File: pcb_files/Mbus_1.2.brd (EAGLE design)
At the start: 101.6 x 71.1 mm, 50 parts, among them IC1 NCP1117ST50T3G, IC3 ATMEGA2560-16AU, IC4 RTC_PCF8523T, J1 F-1X18-SIP-100-32Y, J2 USB_A_SMT_FEMALE, M1 SERVO, Q1 BSS138, Q2 32.768, Q3 BSS138, Y1 CSTCE16M0V53-R0 16MHZ

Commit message: Modify the npn transistor and board layout for 1.2
Signed-off-by: Yiteng Cai <alonsochate@umich.edu>
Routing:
- net PD7: track 121.3 -> 46.4 mm, vias 2 -> 0
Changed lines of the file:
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@@
 <drawing>
 <settings>
-<setting alwaysvectorfont="no"/>
+<setting alwaysvectorfont="yes"/>
 <setting keepoldvectorfont="yes"/>
 <setting verticaltext="up"/>
@@
 <wire x1="96.57588125" y1="36.41851875" x2="96.57588125" y2="34.65321875" width="0.2032" layer="1"/>
 <wire x1="97.6376" y1="35.3568" x2="98.552" y2="35.306" width="0.2032" layer="1"/>
-<wire x1="13.1064" y1="18.1864" x2="13.1064" y2="17.26235625" width="0.2032" layer="1"/>
-<wire x1="13.8176" y1="18.8976" x2="13.1064" y2="18.1864" width="0.2032" layer="1"/>
-<wire x1="13.8176" y1="19.1008" x2="13.8176" y2="18.8976" width="0.2032" layer="1"/>
-<wire x1="35.9664" y1="19.1008" x2="13.8176" y2="19.1008" width="0.2032" layer="16"/>
-<wire x1="68.7832" y1="51.9176" x2="35.9664" y2="19.1008" width="0.2032" layer="16"/>
-<wire x1="71.3232" y1="51.9176" x2="68.7832" y2="51.9176" width="0.2032" layer="16"/>
-<wire x1="71.9328" y1="52.5272" x2="71.3232" y2="51.9176" width="0.2032" layer="1"/>
-<wire x1="72.7456" y1="52.5272" x2="71.9328" y2="52.5272" width="0.2032" layer="1"/>
 <wire x1="72.7456" y1="52.5272" x2="72.77" y2="52.482" width="0.2032" layer="1"/>
-<via x="13.8176" y="19.1008" extent="1-16" drill="0.4064"/>
-<via x="71.3232" y="51.9176" extent="1-16" drill="0.4064"/>
 </signal>
 <signal name="+3V3">

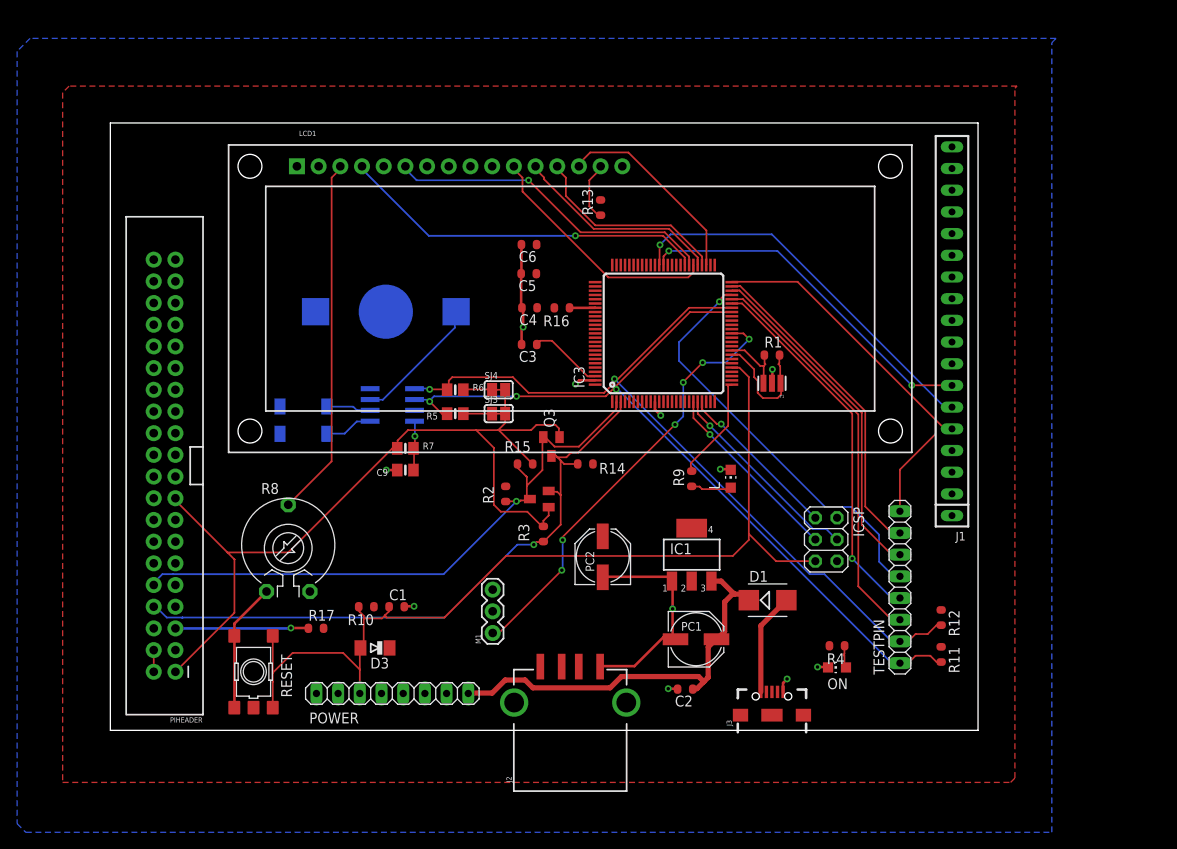
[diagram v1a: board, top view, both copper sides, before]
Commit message: Modify trace width. Not finished on the board layout.
Signed-off-by: Yiteng Cai <alonsochate@umich.edu>
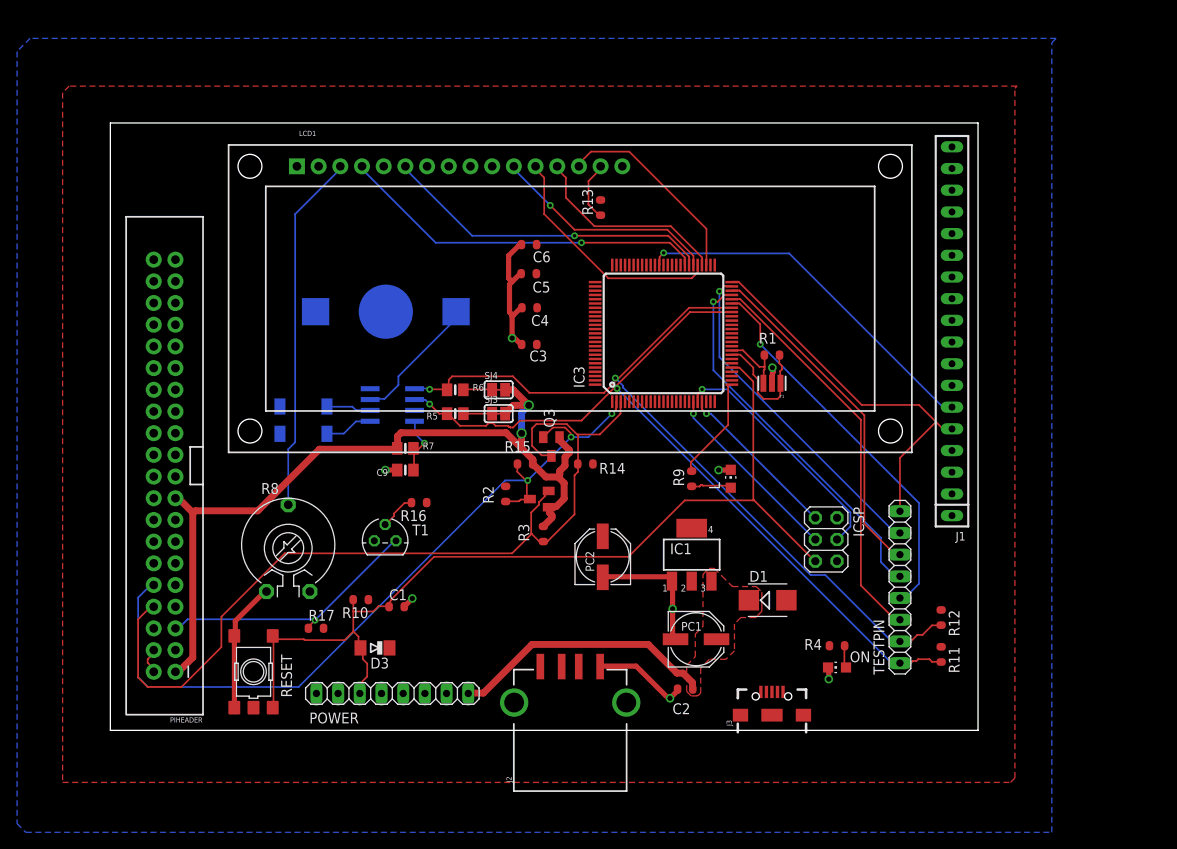
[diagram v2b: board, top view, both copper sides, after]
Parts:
- removed M1: SERVO, SparkFun-Electromechanical:1X03
- added T1: 2N3904, transistor:TO92
- moved R16 28.3 mm to (36.2, 26.7)
- moved R10 1.05 mm to (29.3, 15.3)
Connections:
- net +5V: no longer M1.2
- net GND: now also T1.3; no longer M1.3
- net N$4: now also T1.2
- net OUT: now also T1.1
- net PL3: no longer M1.1
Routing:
- net PL3: track 51.2 -> 0.00 mm, vias 6 -> 0
- net RXD3: track 41.6 -> 0.00 mm, vias 2 -> 0
- net TXD0: track 76.1 -> 105.8 mm, vias 1 -> 0
- net RXD0: track 72.9 -> 95.2 mm, vias 1 -> 3
- net VIN: track 48.2 -> 31.3 mm
- net OUT: track 15.6 -> 31.6 mm
- net PWRIN: track 12.0 -> 0.00 mm
- net AREF: track 8.76 -> 0.00 mm
- net +3V3: track 103.3 -> 97.8 mm, vias 0 -> 2
- net PB2: track 23.8 -> 28.8 mm
- net PD4: track 49.0 -> 44.1 mm
- net N$4: track 0.00 -> 4.37 mm
- net PC2: track 24.7 -> 28.3 mm
- net N$1: track 3.01 -> 0.00 mm
- net TXD3: track 45.5 -> 42.9 mm
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- added copper zone on layer 1, net VIN

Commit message: Save
Signed-off-by: Yiteng Cai <alonsochate@umich.edu>
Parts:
- moved R2 10.6 mm to (52.3, 36.4)
- moved R3 8.99 mm to (45.8, 30.5)
- moved Q3 6.35 mm to (56.7, 29.3), turned to 270 degrees
- moved R14 5.70 mm to (60.4, 34.3)
- moved R15 5.58 mm to (52.4, 27.2), turned to 90 degrees
- moved Q1 5.25 mm to (50.2, 32.3), turned to 270 degrees
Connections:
- new net N$12: PIHEADER.10, Q3.2, R15.1
- new net N$5: PIHEADER.8, Q1.2, R3.1
- net RXD0: no longer PIHEADER.10, Q3.2, R15.1
- net TXD0: no longer PIHEADER.8, Q1.2, R3.1
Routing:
- net TXD0: track 105.8 -> 5.75 mm
- net RXD0: track 95.2 -> 3.66 mm, vias 3 -> 0
- net N$12: track 0.00 -> 75.7 mm, vias 0 -> 1
- net N$5: track 0.00 -> 73.8 mm
- net TXD1: track 46.6 -> 0.00 mm
- net RXD1: track 45.4 -> 0.00 mm, vias 1 -> 0
- net PD4: track 44.1 -> 0.00 mm, vias 1 -> 0
- net PC5: track 43.3 -> 0.00 mm, vias 1 -> 0
- net TXD3: track 42.9 -> 0.00 mm, vias 1 -> 0
- net PD5: track 40.0 -> 0.00 mm
- net PD6: track 39.1 -> 0.00 mm, vias 1 -> 0
- net PC4: track 38.8 -> 0.00 mm, vias 1 -> 0
- net PB2: track 28.8 -> 0.00 mm, vias 1 -> 0
- net PC2: track 28.3 -> 0.00 mm
- net +3V3: track 97.8 -> 70.4 mm, vias 2 -> 0
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- added copper zone on layer 1, net +3V3

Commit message: Save
Signed-off-by: Yiteng Cai <alonsochate@umich.edu>
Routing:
- net TXD1: track 0.00 -> 48.9 mm, vias 0 -> 1
- net PD4: track 0.00 -> 44.0 mm, vias 0 -> 1
- net RXD1: track 0.00 -> 43.9 mm
- net PC5: track 0.00 -> 43.3 mm, vias 0 -> 1
- net TXD3: track 0.00 -> 42.9 mm, vias 0 -> 1
- net RXD3: track 0.00 -> 40.1 mm, vias 0 -> 2
- net PD5: track 0.00 -> 40.0 mm
- net PD6: track 0.00 -> 39.2 mm, vias 0 -> 1
- net PC4: track 0.00 -> 38.8 mm, vias 0 -> 1
- net N$1: track 0.00 -> 33.2 mm, vias 0 -> 2
- net SCL: track 77.1 -> 108.0 mm, vias 1 -> 2
- net PC2: track 0.00 -> 29.2 mm
- net PB2: track 0.00 -> 28.8 mm, vias 0 -> 1
- net RESET: track 88.0 -> 115.3 mm
- net PC3: track 0.00 -> 26.7 mm, vias 0 -> 1
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
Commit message: Create gerber files
Signed-off-by: Yiteng Cai <alonsochate@umich.edu>
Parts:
- moved C5 7.73 mm to (53.5, 59.8)
- moved IC3 7.73 mm to (69.3, 52.8)
- moved LCD1 7.73 mm to (58.3, 56.8)
- moved Q1 7.73 mm to (54.7, 38.6)
- moved R9 7.73 mm to (72.6, 35.8)
- moved C1 7.73 mm to (38.0, 20.8)
- moved C2 7.73 mm to (71.8, 11.1)
- moved C9 7.73 mm to (39.0, 36.8)
- moved D3 7.73 mm to (35.5, 15.9)
- moved ICSP 7.73 mm to (88.3, 28.6)
- moved ON 7.73 mm to (89.6, 13.7)
- moved PC1 7.73 mm to (73.1, 17.0)
- moved R11 7.73 mm to (101.8, 15.2)
- moved R15 7.73 mm to (56.9, 33.4)
- moved R17 7.73 mm to (28.6, 18.2)
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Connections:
- removed net RXD2: IC3.12
- removed net TXD2: IC3.13
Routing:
- net OUT: track 37.5 -> 89.9 mm
- net N$12: track 75.7 -> 60.3 mm
- net +3V3: track 71.3 -> 80.5 mm
- net GND: track 92.4 -> 100.6 mm
- net PWRIN: track 12.0 -> 18.2 mm
- net N$5: track 71.3 -> 69.1 mm
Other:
- board size 101.6 x 71.1 mm -> 113 x 78.7 mm

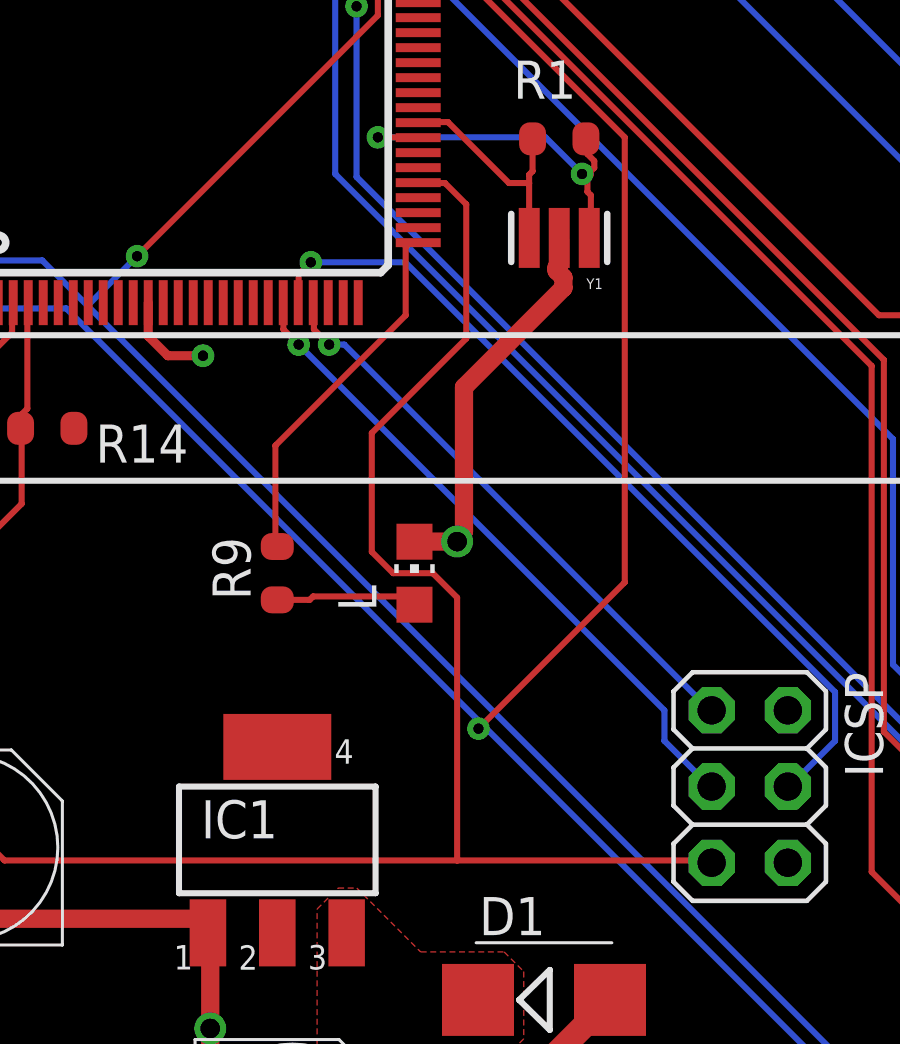
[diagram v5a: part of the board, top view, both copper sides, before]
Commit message: Modify one trace
Signed-off-by: Yiteng Cai <alonsochate@umich.edu>
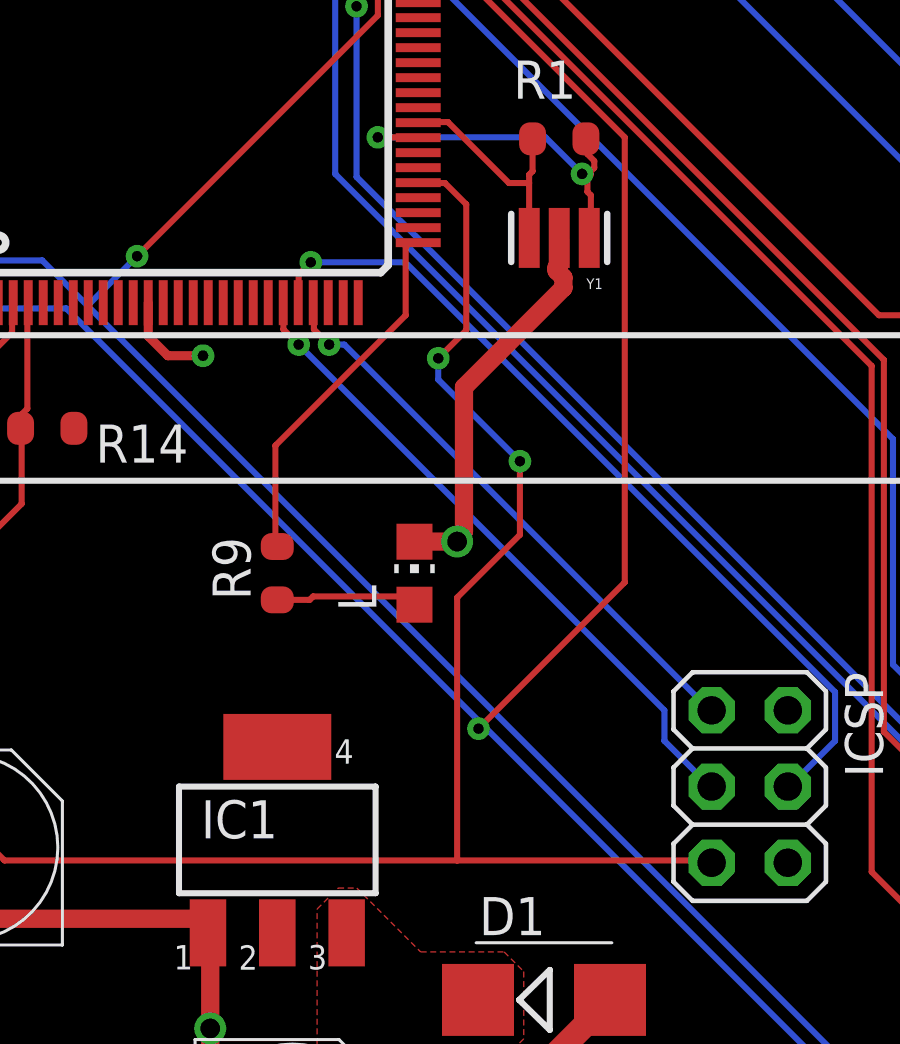
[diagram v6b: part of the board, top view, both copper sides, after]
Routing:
- net RESET: track 115.3 -> 114.4 mm, vias 0 -> 2
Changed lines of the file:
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@@
 <wire x1="33.9852" y1="15.4305" x2="33.7838" y2="15.9385" width="0.2032" layer="1"/>
 <wire x1="78.1558" y1="48.7553" x2="77.343" y2="48.7553" width="0.2032" layer="1"/>
-<wire x1="78.867" y1="48.0441" x2="78.1558" y2="48.7553" width="0.2032" layer="1"/>
-<wire x1="78.867" y1="43.5737" x2="78.867" y2="48.0441" width="0.2032" layer="1"/>
-<wire x1="75.7174" y1="40.4241" x2="78.867" y2="43.5737" width="0.2032" layer="1"/>
-<wire x1="75.7174" y1="36.4617" x2="75.7174" y2="40.4241" width="0.2032" layer="1"/>
-<wire x1="76.4286" y1="35.7505" x2="75.7174" y2="36.4617" width="0.2032" layer="1"/>
-<wire x1="77.7494" y1="35.7505" x2="76.4286" y2="35.7505" width="0.2032" layer="1"/>
-<wire x1="78.5622" y1="34.9377" x2="77.7494" y2="35.7505" width="0.2032" layer="1"/>
-<wire x1="78.5622" y1="26.1747" x2="78.5622" y2="34.9377" width="0.2032" layer="1"/>
+<wire x1="78.1558" y1="48.7553" x2="78.867" y2="48.0441" width="0.2032" layer="1"/>
+<wire x1="78.5622" y1="34.9377" x2="78.5622" y2="26.1747" width="0.2032" layer="1"/>
 <wire x1="77.343" y1="48.7553" x2="77.2658" y2="48.7685" width="0.2032" layer="1"/>
 <wire x1="33.7838" y1="15.9385" x2="23.7083625" y2="15.9385" width="0.2032" layer="1"/>
@@
 <wire x1="32.9653" y1="20.6844" x2="32.9565" y2="20.6756" width="0.2032" layer="1"/>
 <wire x1="35.0950875" y1="20.6844" x2="32.9653" y2="20.6844" width="0.2032" layer="1"/>
+<wire x1="78.867" y1="48.0441" x2="78.867" y2="43.84801875" width="0.2032" layer="1"/>
+<wire x1="78.867" y1="43.84801875" x2="77.93228125" y2="42.9133" width="0.2032" layer="1"/>
+<via x="77.93228125" y="42.9133" extent="1-16" drill="0.35"/>
+<wire x1="77.93228125" y1="42.9133" x2="77.93228125" y2="42.2046375" width="0.2032" layer="16"/>
+<wire x1="77.93228125" y1="42.2046375" x2="80.655159375" y2="39.481759375" width="0.2032" layer="16"/>
+<via x="80.655159375" y="39.481759375" extent="1-16" drill="0.35"/>
+<wire x1="80.655159375" y1="39.481759375" x2="80.655159375" y2="37.030659375" width="0.2032" layer="1"/>
+<wire x1="80.655159375" y1="37.030659375" x2="78.5622" y2="34.9377" width="0.2032" layer="1"/>
 </signal>
 <signal name="VIN" class="1">
